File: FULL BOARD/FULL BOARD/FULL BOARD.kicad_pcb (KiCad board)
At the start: 2 copper layers, 200 x 200 mm, 101 parts, among them IC1 TAS5760LDAP, J1 PJ-036AH-SMT-TR, J2 Micro_SD_Card, J3 B2B-PH-K-S, J4 5019514000, J5 61201021621, J6 B2B-PH-K-S, SW1 PTS645SK50SMTR92LFS, U1 LD1117S33TR_SOT223, U2 STM32H743VITx, Y1 ABLS7M2-16.000MHZ-D-2Y-T

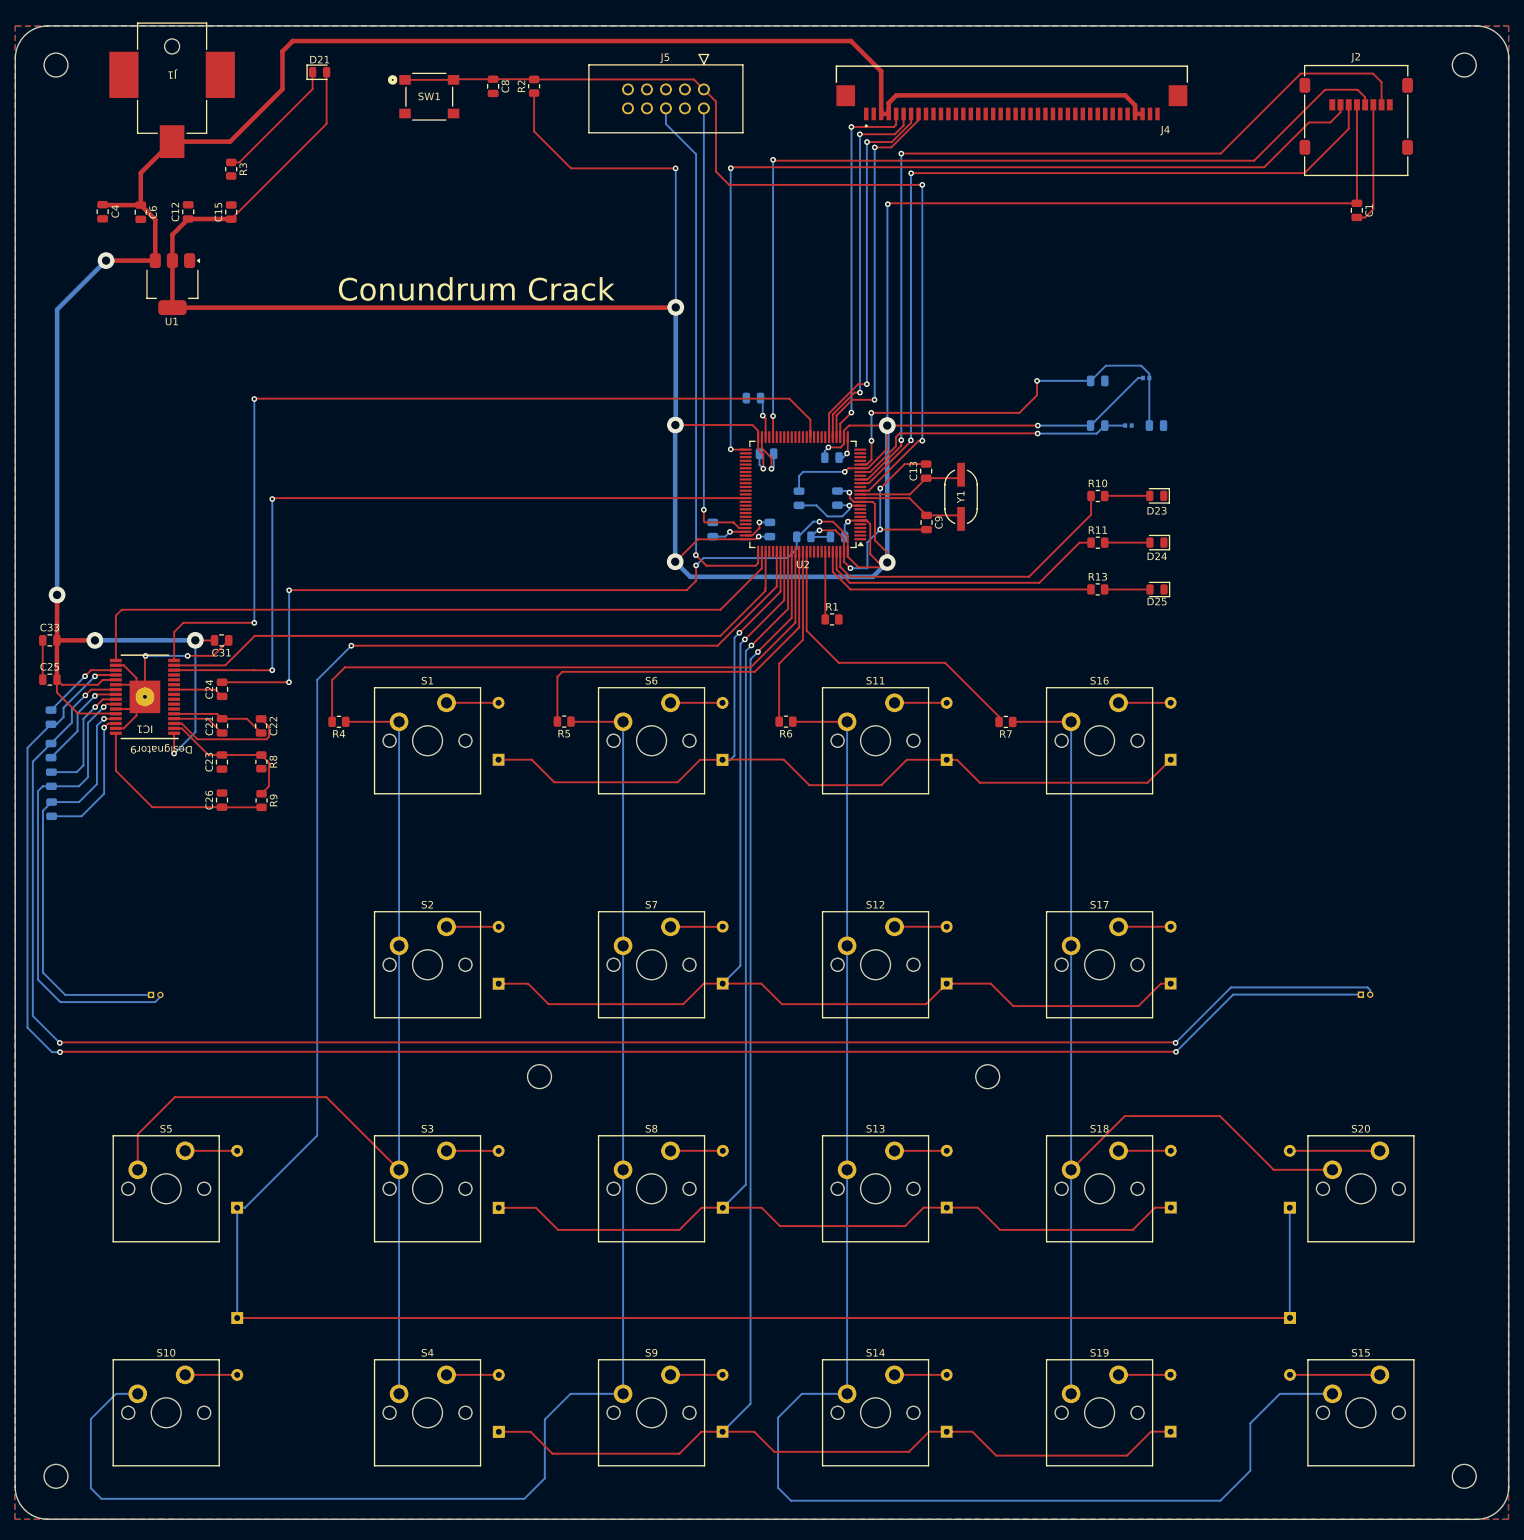
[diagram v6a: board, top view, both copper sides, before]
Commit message: added filters and sleep
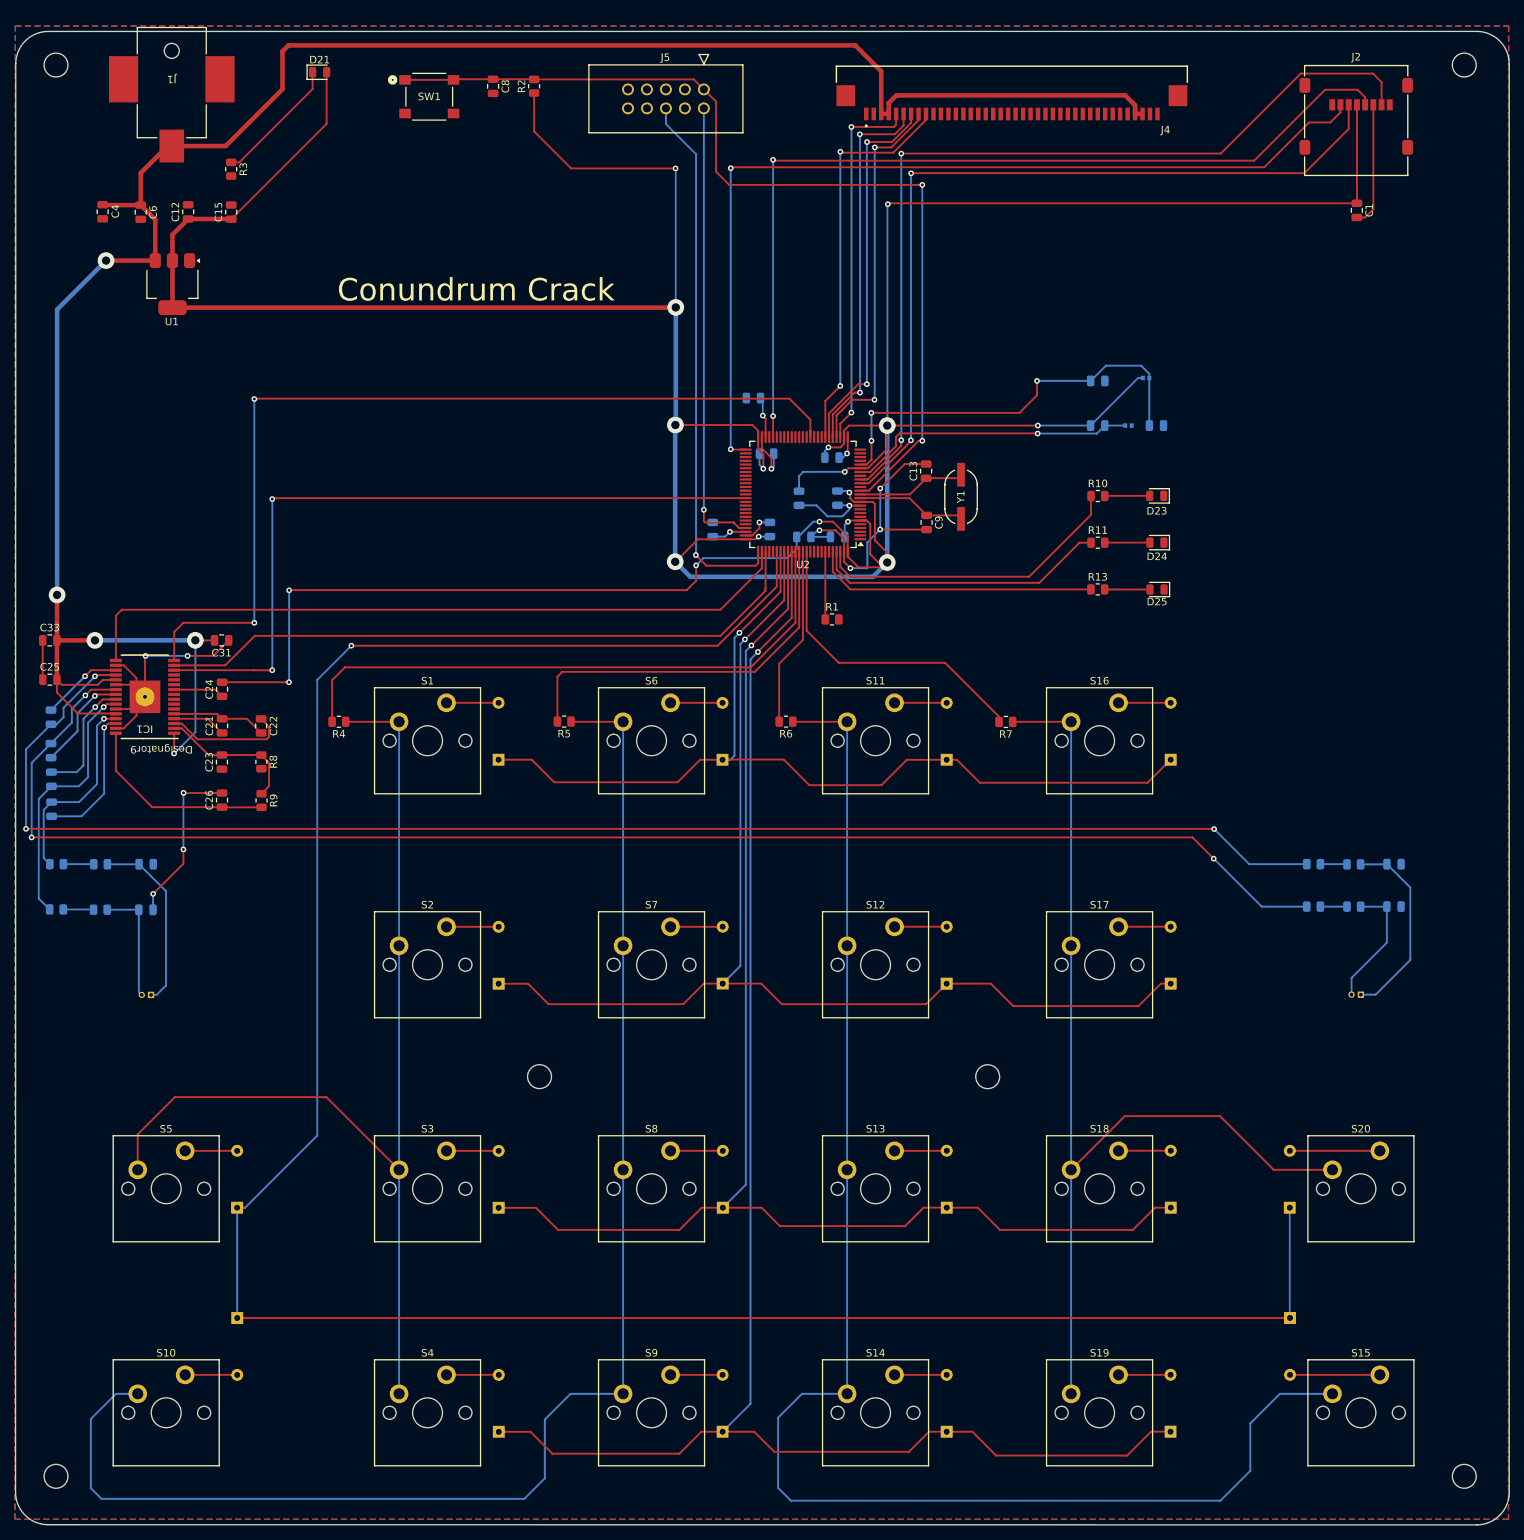
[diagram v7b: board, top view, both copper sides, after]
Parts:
- added C32: 47nF, Capacitor_SMD:C_0805_2012Metric, B.Cu at (86.1, 156.0)
- added C34: 47nF, Capacitor_SMD:C_0805_2012Metric, B.Cu at (86.0, 162.1)
- added C35: 47nF, Capacitor_SMD:C_0805_2012Metric, B.Cu at (253.2, 156.0)
- added C36: 47nF, Capacitor_SMD:C_0805_2012Metric, B.Cu at (253.2, 161.7)
- added R12: 68, Resistor_SMD:R_0805_2012Metric, B.Cu at (80.0, 156.0)
- added R14: 100, Resistor_SMD:R_0805_2012Metric, B.Cu at (74.1, 156.0)
- added R15: 100, Resistor_SMD:R_0805_2012Metric, B.Cu at (74.1, 162.1)
- added R16: 68, Resistor_SMD:R_0805_2012Metric, B.Cu at (79.9, 162.1)
- added R17: 100, Resistor_SMD:R_0805_2012Metric, B.Cu at (242.4, 156.0)
- added R18: 68, Resistor_SMD:R_0805_2012Metric, B.Cu at (247.8, 156.1)
- added R19: 100, Resistor_SMD:R_0805_2012Metric, B.Cu at (242.4, 161.7)
- added R20: 68, Resistor_SMD:R_0805_2012Metric, B.Cu at (247.8, 161.7)
- moved J1 0.60 mm to (89.5, 51.4)
- turned J3 to 0 degrees
- turned J6 to 0 degrees
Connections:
- J3 pad 1: Net-(IC1-SPK_OUTA+) -> Net-(C32-Pad2)
- J3 pad 2: Net-(IC1-SPK_OUTA-) -> Net-(C34-Pad1)
- J4 pad 9: unconnected-(J4-Pad9) -> Wait
- J6 pad 1: Net-(IC1-SPK_OUTB+) -> Net-(C35-Pad2)
- J6 pad 2: Net-(IC1-SPK_OUTB-) -> Net-(C36-Pad1)
- U2 pad 32: unconnected-(U2-PC4-Pad32) -> Wait
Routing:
- net Wait: track 0.00 -> 53.2 mm, vias 0 -> 2
- net Net-(IC1-SPK_OUTB+): track 237.3 -> 201.0 mm
- net Net-(IC1-SPK_OUTB-): track 234.7 -> 201.0 mm
- net Net-(IC1-SPK_OUTA+): track 56.8 -> 26.9 mm
- net Net-(IC1-SPK_OUTA-): track 63.0 -> 35.3 mm
- net Net-(C35-Pad2): track 0.00 -> 26.2 mm
- net Net-(C32-Pad2): track 0.00 -> 24.5 mm
- net GND: track 120.8 -> 143.3 mm, vias 10 -> 13
- net Net-(C36-Pad1): track 0.00 -> 17.3 mm
- net Net-(C34-Pad1): track 0.00 -> 15.8 mm
- net Net-(R15-Pad2): track 0.00 -> 4.07 mm
- net Net-(R12-Pad1): track 0.00 -> 4.06 mm
- net Net-(R17-Pad2): track 0.00 -> 3.57 mm
- net Net-(R19-Pad2): track 0.00 -> 3.57 mm
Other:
- outline, holes or cut-outs redrawn

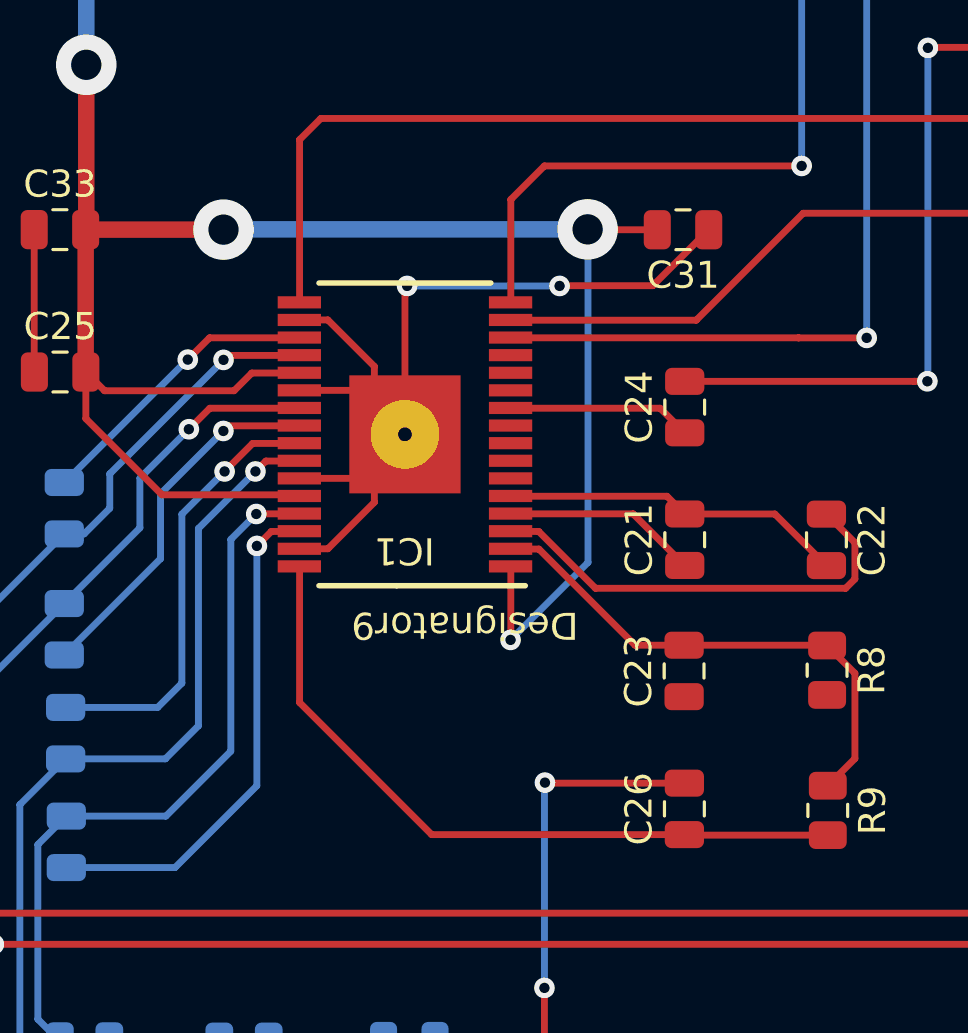
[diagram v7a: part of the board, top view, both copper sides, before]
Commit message: changed amp via
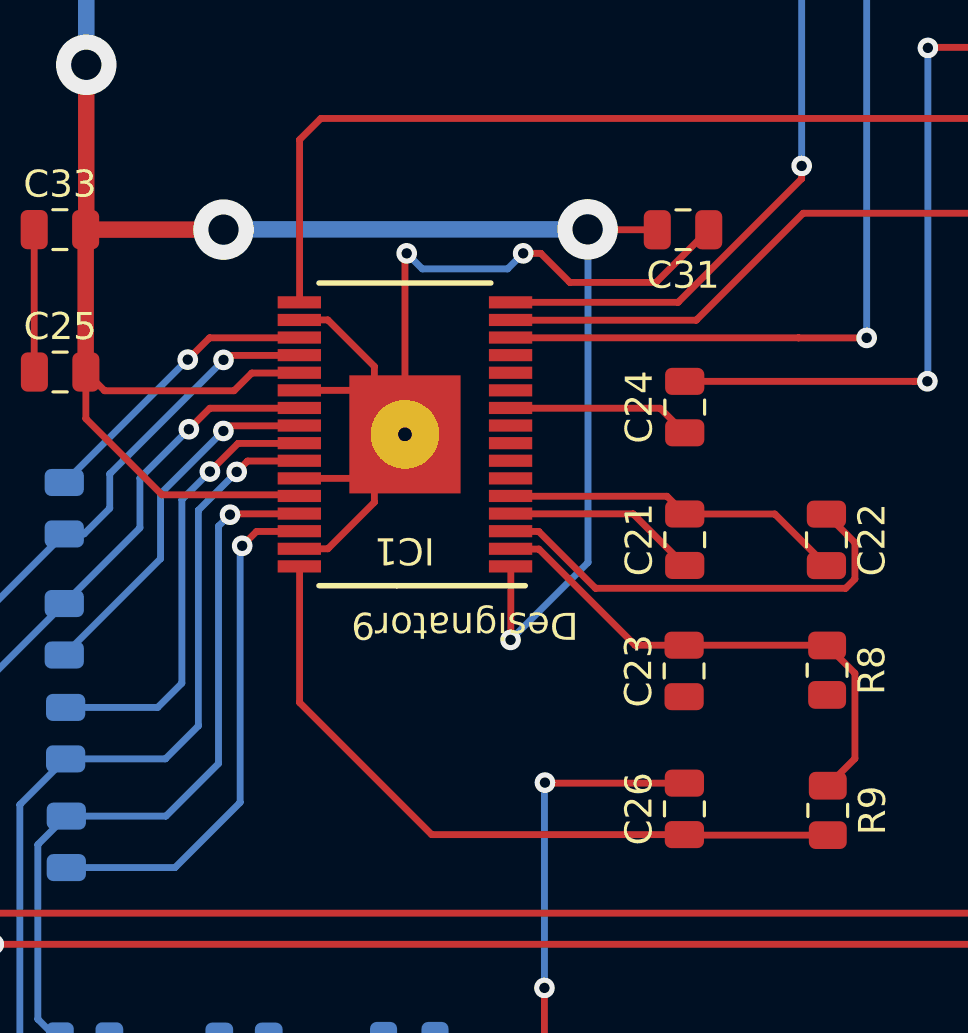
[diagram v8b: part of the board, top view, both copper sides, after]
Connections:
- IC1 pad V: (no net) -> GND
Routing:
- net GND: track 143.3 -> 145.4 mm
- net I2S_SD: track 123.9 -> 122.0 mm
- net Net-(IC1-SPK_OUTA+): track 26.9 -> 27.5 mm
